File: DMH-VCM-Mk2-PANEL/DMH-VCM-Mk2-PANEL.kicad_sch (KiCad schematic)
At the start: 27 parts, among them J0 Panel_GND_Solder_Wire_Pad

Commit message: Updated symbols and fps as per library
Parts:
- H19, H20, H21: footprint SynthStuff:Toggle_Switch_Cutout -> SynthStuff:Toggle_Switch_TE_Cutout
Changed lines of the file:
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@@
 	)
 	(symbol
+		(lib_name "MountingHole_ToggleSwitch_2")
 		(lib_id "SynthStuff:MountingHole_ToggleSwitch")
 		(at 101.6 139.7 0)
@@
 			)
 		)
-		(property "Footprint" "SynthStuff:Toggle_Switch_Cutout"
+		(property "Footprint" "SynthStuff:Toggle_Switch_TE_Cutout"
 			(at 101.6 139.7 0)
 			(effects
@@
 	)
 	(symbol
+		(lib_name "MountingHole_ToggleSwitch_1")
 		(lib_id "SynthStuff:MountingHole_ToggleSwitch")
 		(at 101.6 203.2 0)
@@
 			)
 		)
-		(property "Footprint" "SynthStuff:Toggle_Switch_Cutout"
+		(property "Footprint" "SynthStuff:Toggle_Switch_TE_Cutout"
 			(at 101.6 203.2 0)
 			(effects
@@
 			)
 		)
-		(property "Footprint" "SynthStuff:Toggle_Switch_Cutout"
+		(property "Footprint" "SynthStuff:Toggle_Switch_TE_Cutout"
 			(at 101.6 88.9 0)
 			(effects

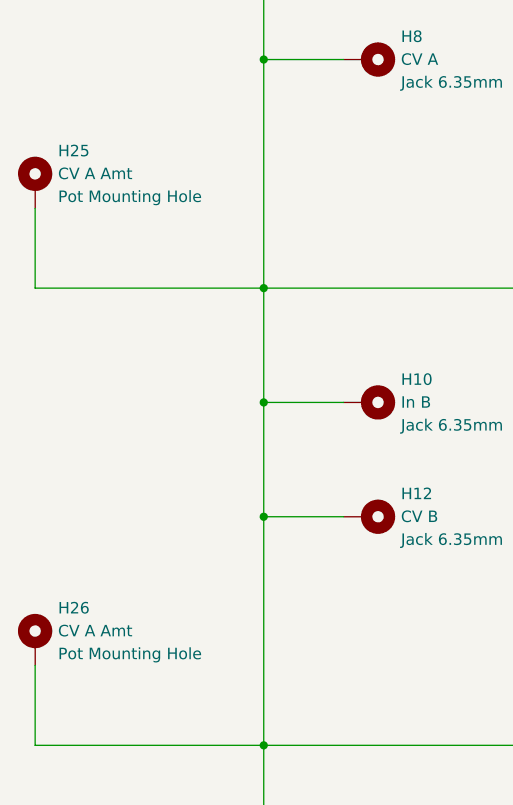
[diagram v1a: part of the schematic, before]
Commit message: Almost finished PCB 1 schematic
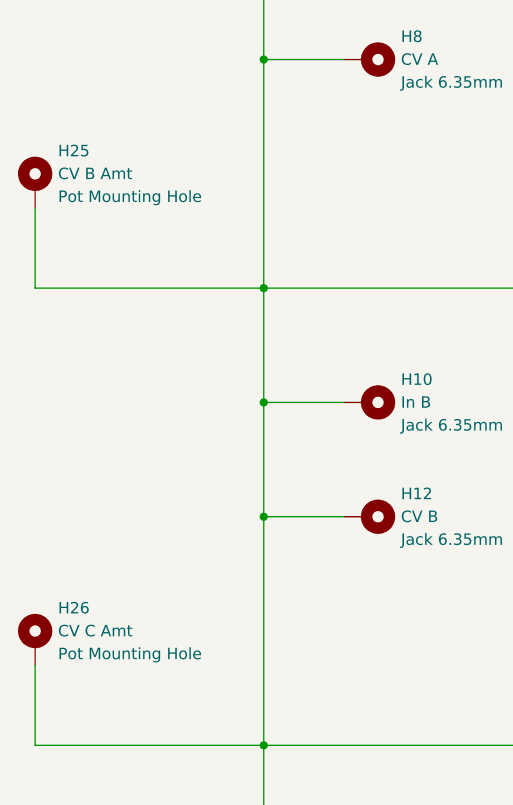
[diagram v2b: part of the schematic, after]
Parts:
- H25: value CV A Amt -> CV B Amt
- H26: value CV A Amt -> CV C Amt
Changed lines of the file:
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@@
 			)
 		)
-		(property "Value" "CV A Amt"
+		(property "Value" "CV B Amt"
 			(at 27.94 101.5999 0)
 			(effects
@@
 			)
 		)
-		(property "Value" "CV A Amt"
+		(property "Value" "CV C Amt"
 			(at 27.94 152.3999 0)
 			(effects

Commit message: Kicad 10 and updated SynthStuff
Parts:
- H17, H22, H23: footprint SynthStuff:MountingHole_LED_3mm -> SynthStuff:MountingHole_LED_3mm_R
